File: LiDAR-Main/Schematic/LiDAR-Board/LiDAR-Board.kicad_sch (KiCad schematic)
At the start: 1 part, among them U1 Pico

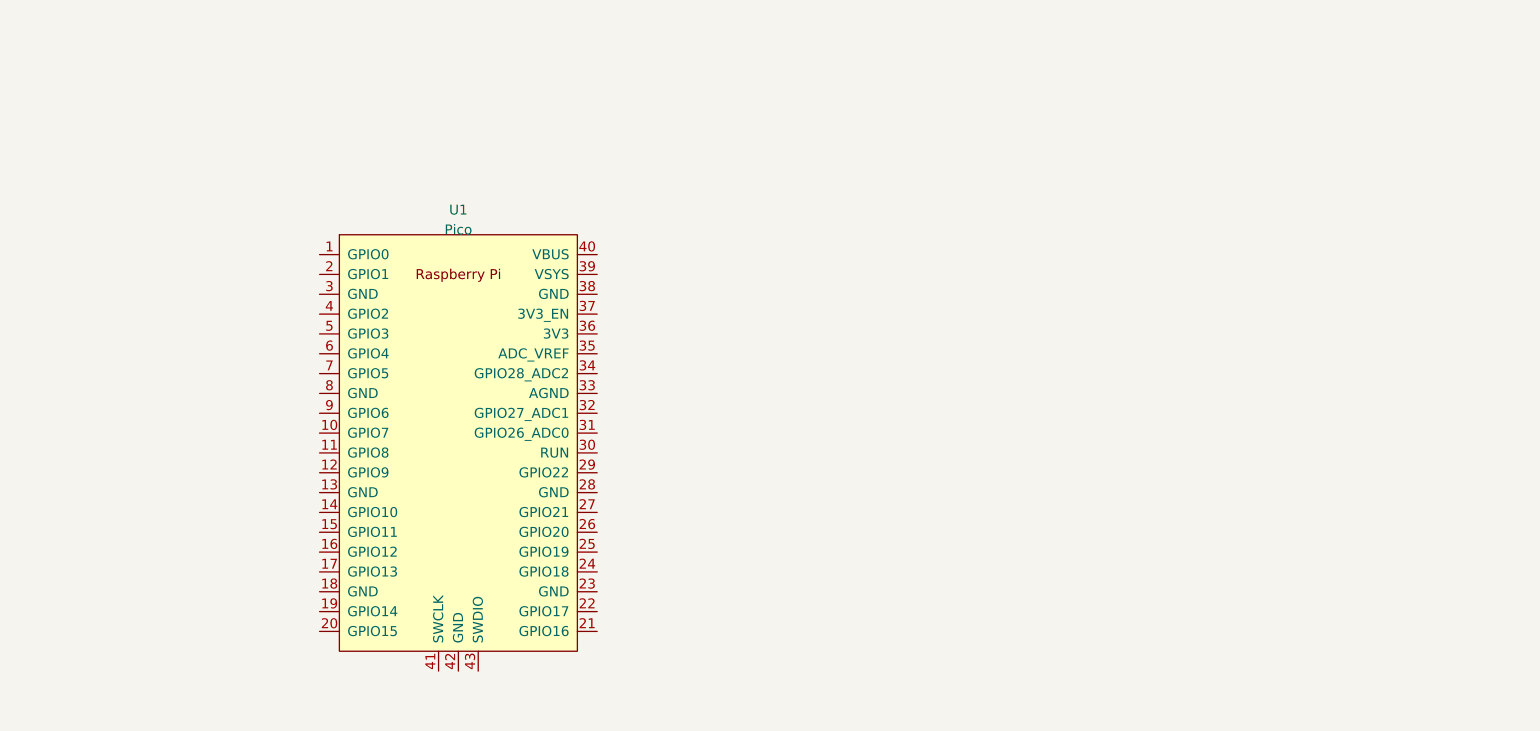
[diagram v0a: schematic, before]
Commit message: Finished LiDAR Schematic
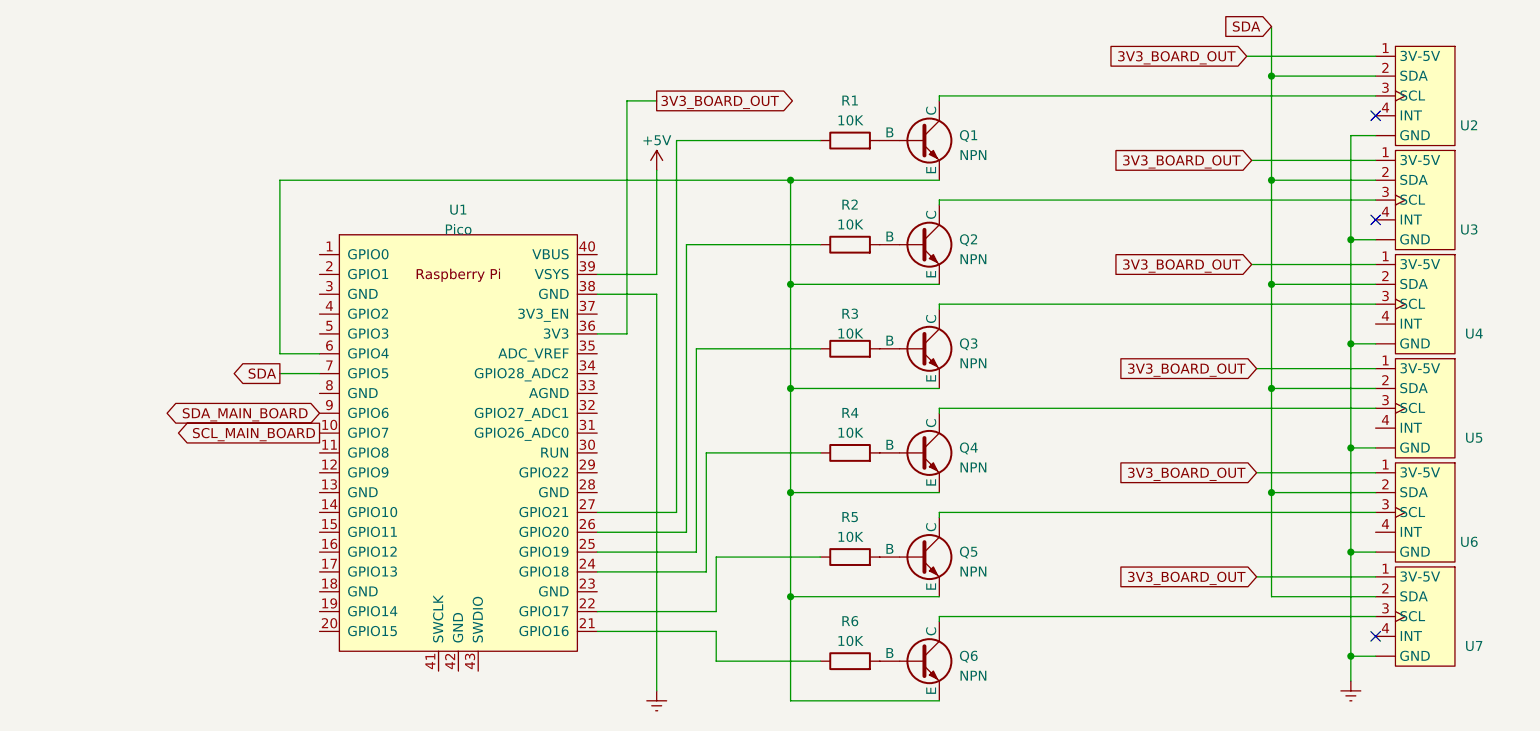
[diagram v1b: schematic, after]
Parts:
- added Q1, Q2, Q3, Q4, Q5, Q6: NPN, symbol Simulation_SPICE:NPN
- added R1, R2, R3, R4, R5, R6: 10K, symbol Device:R
- added U2, U3, U4, U5, U6, U7: ~, symbol VL53L5CX_KiCAD:VL53L5CX_Pimoroni
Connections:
- net SCL_MAIN_BOARD: now reaches U1.10 (GPIO7)
- net at U1.21 (GPIO16): now also R6.1
- net at U1.22 (GPIO17): now also R5.1
- net at U1.24 (GPIO18): now also R4.1
- net at U1.25 (GPIO19): now also R3.1
- net at U1.26 (GPIO20): now also R2.1
- net at U1.27 (GPIO21): now also R1.1
- net 3V3_BOARD_OUT: now reaches U1.36 (3V3)
- net 3V3_BOARD_OUT: now also U2.1 (3V-5V), U3.1 (3V-5V), U4.1 (3V-5V), U5.1 (3V-5V), U6.1 (3V-5V), U7.1 (3V-5V)
- net Earth: now reaches U1.38 (GND)
- net Earth: now also U2. (GND), U3. (GND), U4. (GND), U5. (GND), U6. (GND), U7. (GND)
- net +5V: now reaches U1.39 (VSYS)
- net at U1.6 (GPIO4): now also Q1.3 (E), Q2.3 (E), Q3.3 (E), Q4.3 (E), Q5.3 (E), Q6.3 (E)
- net SDA: now reaches U1.7 (GPIO5)
- net SDA: now also U2.2 (SDA), U3.2 (SDA), U4.2 (SDA), U5.2 (SDA), U6.2 (SDA), U7.2 (SDA)
- net SDA_MAIN_BOARD: now reaches U1.9 (GPIO6)
- new net: Q1.1 (C), U2.3 (SCL)
- new net: Q1.2 (B), R1.2
- new net: Q2.1 (C), U3.3 (SCL)
- new net: Q2.2 (B), R2.2
- new net: Q5.2 (B), R5.2
- new net: Q4.1 (C), U5.3 (SCL)
- new net: Q4.2 (B), R4.2
- new net: Q6.1 (C), U7.3 (SCL)
- new net: Q3.1 (C), U4.3 (SCL)
- new net: Q3.2 (B), R3.2
- new net: Q5.1 (C), U6.3 (SCL)
- new net: Q6.2 (B), R6.2
- no-connect marks 0 -> 3

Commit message: Diagram information ammended
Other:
- company: (none) -> HEVCS
- title: (none) -> LiDAR Connection Diagram
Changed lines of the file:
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@@
 (kicad_sch (version 20230121) (generator eeschema)
   (paper "A4")
+  (title_block
+    (title "LiDAR Connection Diagram")
+    (date "2023-04-10")
+    (company "HEVCS")
+    (comment 1 "Note: RPPico is acting as I2C Master")
+  )
   (junction (at 180.34 91.44) (diameter 0) (color 0 0 0 0)
   )

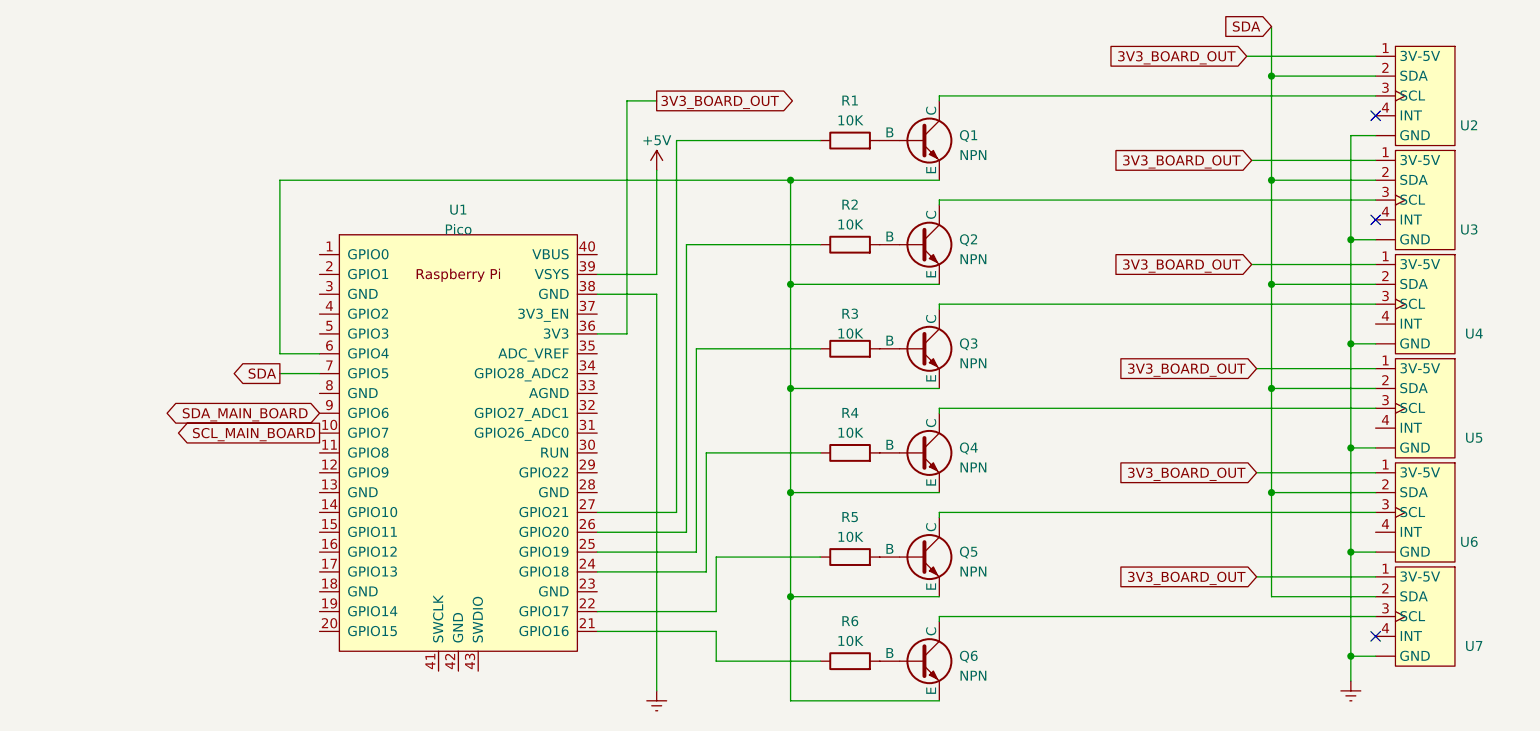
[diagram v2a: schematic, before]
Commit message: partial schematic update
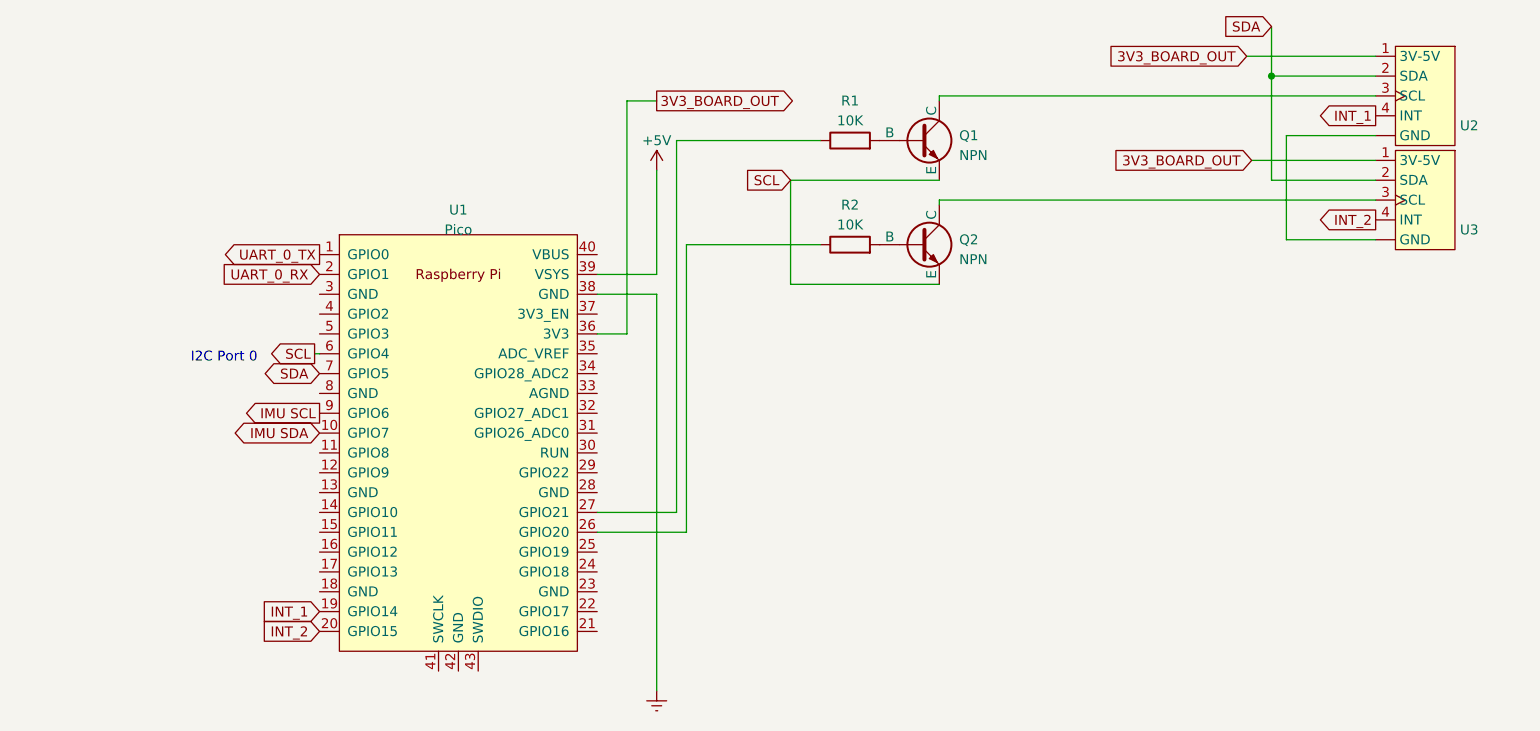
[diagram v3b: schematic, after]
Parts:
- removed Q3, Q4, Q5, Q6: NPN, symbol Simulation_SPICE:NPN
- removed R3, R4, R5, R6: 10K, symbol Device:R
- removed U4, U5, U6, U7: ~, symbol VL53L5CX_KiCAD:VL53L5CX_Pimoroni
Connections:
- net Earth: no longer U2. (GND), U3. (GND)
- net SCL: now reaches Q1.3 (E), Q2.3 (E), U1.6 (GPIO4)
- net INT_2: now reaches U3.4 (INT)
- net INT_2: now also U1.20 (GPIO15)
- net UART_0_TX: now reaches U1.1 (GPIO0)
- net INT_1: now reaches U1.19 (GPIO14)
- net INT_1: now also U2.4 (INT)
- net UART_0_RX: now reaches U1.2 (GPIO1)
- net SCL_MAIN_BOARD renamed IMU SDA
- net SDA_MAIN_BOARD renamed IMU SCL
- new net: U2. (GND), U3. (GND)
- no-connect marks 3 -> 0
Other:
- note added: "I2C Port 0"

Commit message: Updated schematic with MPU6050
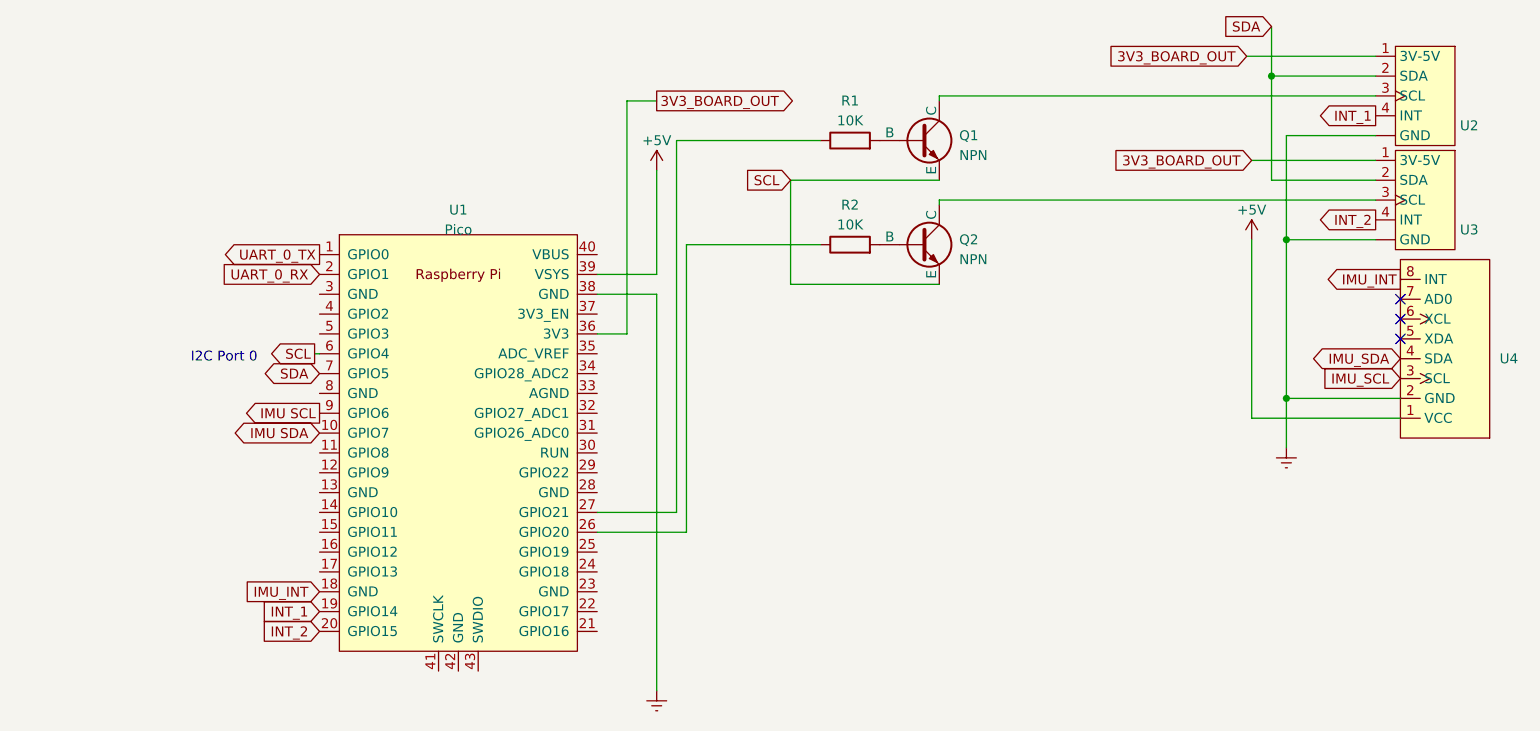
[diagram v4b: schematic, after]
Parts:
- added U4: ~, symbol HEVCS_Sensors:MPU6050
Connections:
- net +5V: now also U4.1 (VCC)
- net Earth: now also U2. (GND), U3. (GND), U4.2 (GND)
- net IMU_INT: now reaches U1.18 (GND)
- net IMU_INT: now also U4.8 (INT)
- new net IMU_SCL: U4.3 (SCL)
- new net IMU_SDA: U4.4 (SDA)
- no-connect marks 0 -> 3
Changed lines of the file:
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@@
   (junction (at 180.34 51.435) (diameter 0) (color 0 0 0 0)
   )
+  (junction (at 182.245 92.71) (diameter 0) (color 0 0 0 0)
+  )
+  (junction (at 182.245 72.39) (diameter 0) (color 0 0 0 0)
+  )
+  (no_connect (at 196.85 80.01))
+  (no_connect (at 196.85 85.09))
+  (no_connect (at 196.85 82.55))
   (wire (pts (xy 137.795 67.31) (xy 193.675 67.31))
     (stroke (width 0) (type default))
@@
     (stroke (width 0) (type default))
   )
+  (wire (pts (xy 196.85 95.25) (xy 177.8 95.25))
+    (stroke (width 0) (type default))
+  )
   (wire (pts (xy 104.14 59.69) (xy 122.555 59.69))
     (stroke (width 0) (type default))
@@
     (stroke (width 0) (type default))
   )
+  (wire (pts (xy 177.8 72.39) (xy 177.8 95.25))
+    (stroke (width 0) (type default))
+  )
+  (wire (pts (xy 182.245 92.71) (xy 182.245 99.06))
+    (stroke (width 0) (type default))
+  )
+  (wire (pts (xy 196.85 92.71) (xy 182.245 92.71))
+    (stroke (width 0) (type default))
+  )
   (wire (pts (xy 177.165 48.895) (xy 193.675 48.895))
+    (stroke (width 0) (type default))
+  )
+  (wire (pts (xy 182.245 72.39) (xy 182.245 92.71))
     (stroke (width 0) (type default))
   )
@@
     )
   )
+  (global_label "IMU_SDA" (shape bidirectional) (at 196.85 87.63 180) (fields_autoplaced)
+    (effects (font (size 1.27 1.27)) (justify right))
+    (property "Intersheetrefs" "${INTERSHEET_REFS}" (at 184.9105 87.63 0)
+      (effects (font (size 1.27 1.27)) (justify right) hide)
+    )
+  )
+  (global_label "IMU_SCL" (shape input) (at 196.85 90.17 180) (fields_autoplaced)
+    (effects (font (size 1.27 1.27)) (justify right))
+    (property "Intersheetrefs" "${INTERSHEET_REFS}" (at 186.0823 90.17 0)
+      (effects (font (size 1.27 1.27)) (justify right) hide)
+    )
+  )
   (global_label "INT_1" (shape input) (at 58.42 120.015 180) (fields_autoplaced)
     (effects (font (size 1.27 1.27)) (justify right))
@@
     )
   )
+  (global_label "IMU_INT" (shape input) (at 58.42 117.475 180) (fields_autoplaced)
+    (effects (font (size 1.27 1.27)) (justify right))
+    (property "Intersheetrefs" "${INTERSHEET_REFS}" (at 48.257 117.475 0)
+      (effects (font (size 1.27 1.27)) (justify right) hide)
+    )
+  )
   (global_label "UART_0_RX" (shape input) (at 58.42 76.835 180) (fields_autoplaced)
     (effects (font (size 1.27 1.27)) (justify right))
@@
     (effects (font (size 1.27 1.27)) (justify right))
     (property "Intersheetrefs" "${INTERSHEET_REFS}" (at 185.6892 56.515 0)
+      (effects (font (size 1.27 1.27)) (justify right) hide)
+    )
+  )
+  (global_label "IMU_INT" (shape output) (at 196.85 77.47 180) (fields_autoplaced)
+    (effects (font (size 1.27 1.27)) (justify right))
+    (property "Intersheetrefs" "${INTERSHEET_REFS}" (at 186.687 77.47 0)
       (effects (font (size 1.27 1.27)) (justify right) hide)
     )
@@
         (path "/379f291a-31d3-4ed1-aaf1-b1b6ffabef49"
           (reference "R2") (unit 1)
+        )
+      )
+    )
+  )
+  (symbol (lib_id "HEVCS_Sensors:MPU6050") (at 209.55 99.06 180) (unit 1)
+    (in_bom yes) (on_board yes) (dnp no) (fields_autoplaced)
+    (property "Reference" "U4" (at 209.55 87.63 0)
+      (effects (font (size 1.27 1.27)) (justify right))
+    )
+    (property "Value" "~" (at 209.55 99.06 0)
+      (effects (font (size 1.27 1.27)))
+    )
+    (property "Footprint" "" (at 209.55 99.06 0)
+      (effects (font (size 1.27 1.27)) hide)
+    )
+    (property "Datasheet" "" (at 209.55 99.06 0)
+      (effects (font (size 1.27 1.27)) hide)
+    )
+    (pin "1")
+    (pin "2")
+    (pin "3")
+    (pin "4")
+    (pin "5")
+    (pin "6")
+    (pin "7")
+    (pin "8")
+    (instances
+      (project "LiDAR-Board"
+        (path "/379f291a-31d3-4ed1-aaf1-b1b6ffabef49"
+          (reference "U4") (unit 1)
         )
       )
@@
         )
       )
+    )
+  )
+  (symbol (lib_id "power:+5V") (at 177.8 72.39 0) (unit 1)
+    (in_bom yes) (on_board yes) (dnp no) (fields_autoplaced)
+    (property "Reference" "#PWR01" (at 177.8 76.2 0)
+      (effects (font (size 1.27 1.27)) hide)
+    )
+    (property "Value" "+5V" (at 177.8 68.58 0)
+      (effects (font (size 1.27 1.27)))
+    )
+    (property "Footprint" "" (at 177.8 72.39 0)
+      (effects (font (size 1.27 1.27)) hide)
+    )
+    (property "Datasheet" "" (at 177.8 72.39 0)
+      (effects (font (size 1.27 1.27)) hide)
+    )
+    (pin "1")
+    (instances
+      (project "LiDAR-Board"
+        (path "/379f291a-31d3-4ed1-aaf1-b1b6ffabef49"
+          (reference "#PWR01") (unit 1)
+        )
+      )
+    )
+  )
+  (symbol (lib_id "power:Earth") (at 182.245 99.06 0) (unit 1)
+    (in_bom yes) (on_board yes) (dnp no) (fields_autoplaced)
+    (property "Reference" "#PWR04" (at 182.245 105.41 0)
+      (effects (font (size 1.27 1.27)) hide)
+    )
+    (property "Value" "Earth" (at 182.245 102.87 0)
+      (effects (font (size 1.27 1.27)) hide)
+    )
+    (property "Footprint" "" (at 182.245 99.06 0)
+      (effects (font (size 1.27 1.27)) hide)
+    )
+    (property "Datasheet" "~" (at 182.245 99.06 0)
+      (effects (font (size 1.27 1.27)) hide)
+    )
+    (pin "1")
+    (instances
+      (project "LiDAR-Board"
+        (path "/379f291a-31d3-4ed1-aaf1-b1b6ffabef49"
+          (reference "#PWR04") (unit 1)
+        )
+      )
